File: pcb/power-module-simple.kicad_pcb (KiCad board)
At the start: 4 copper layers, 55 x 55 mm, 43 parts, among them J1 USB_C_PowerOnly_6P, J2 Power, U1 AZ1084-3.3, U2 LM66200DRLR

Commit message: Attribute updates; generated production files
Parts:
- R3, R4: footprint Resistor_SMD:R_0805_2012Metric -> Resistor_SMD:R_0603_1608Metric
- moved FID1 47.0 mm to (54.0, 156.0)

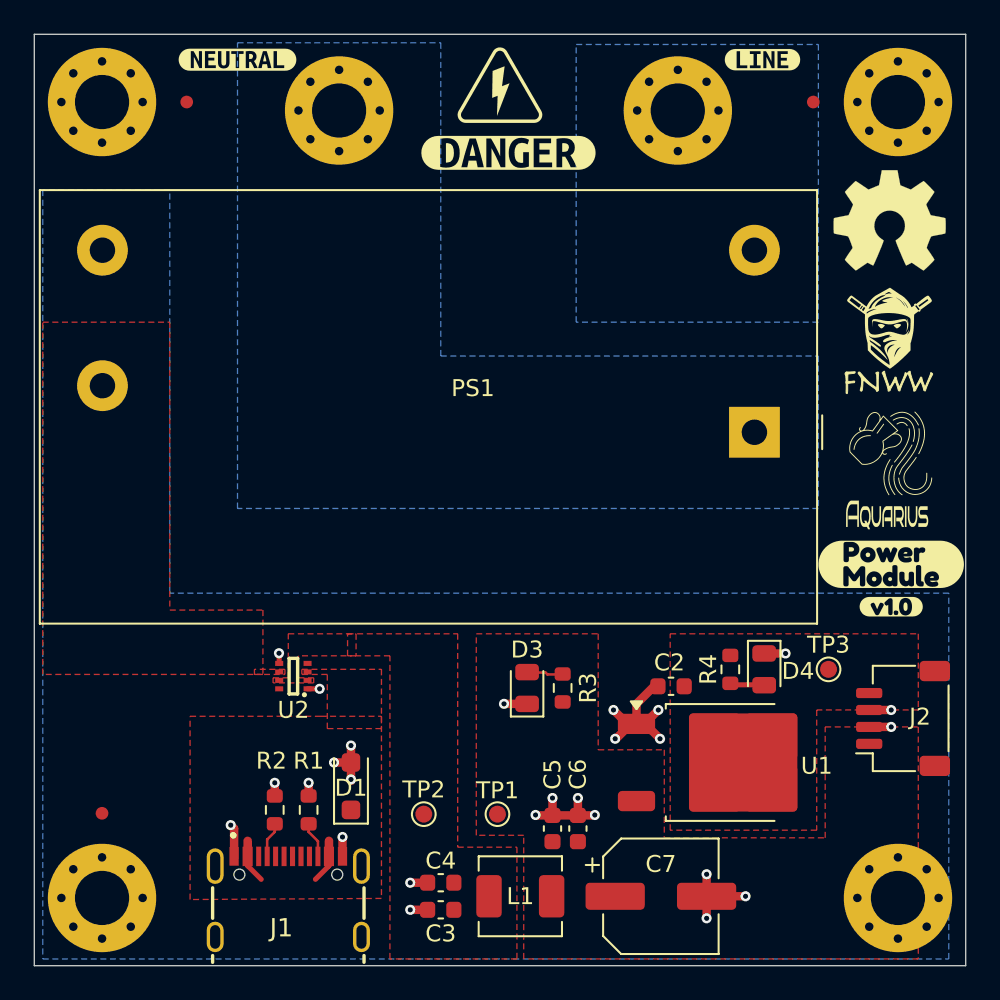
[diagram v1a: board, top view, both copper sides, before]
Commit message: Updated silkscreen and LED size
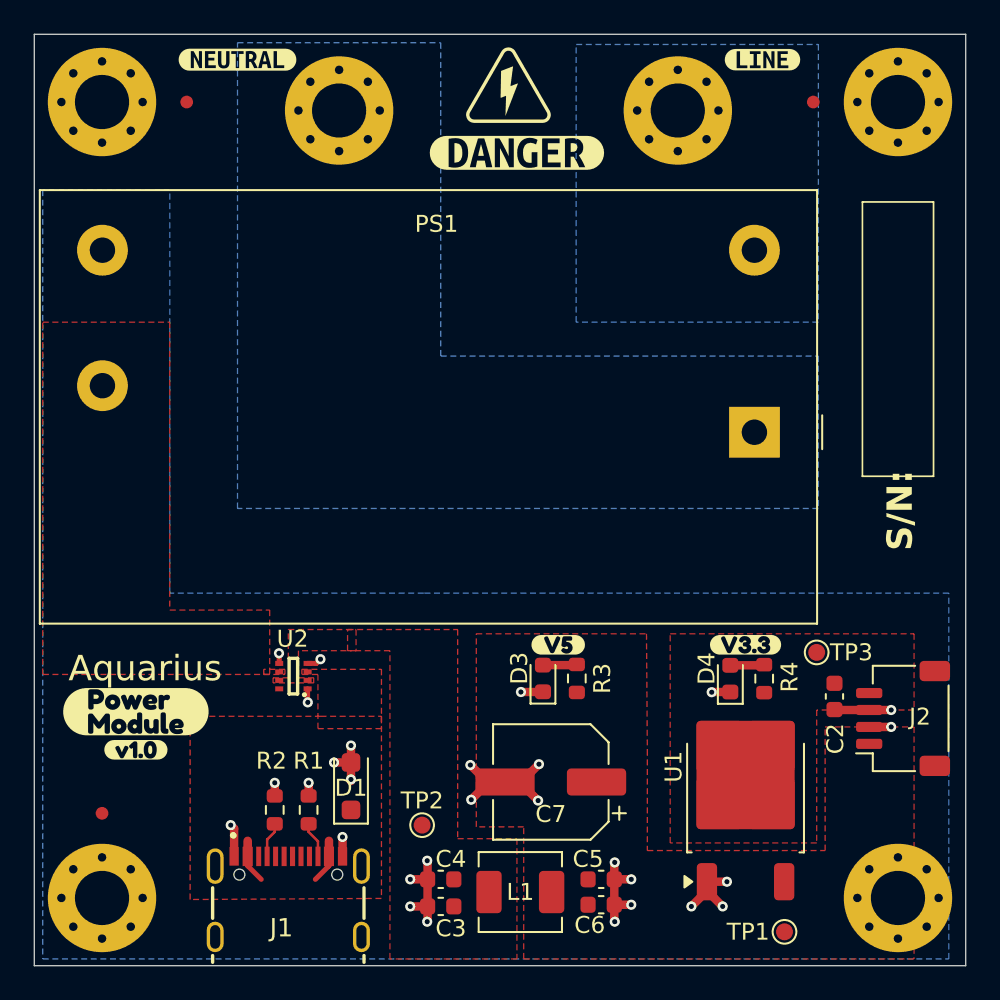
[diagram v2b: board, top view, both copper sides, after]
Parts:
- removed LOGO4: ~, CRGM Logos:FNWW Name 2mmx5mm
- removed LOGO5: ~, CRGM Logos:Aquarius Name 2mmx5mm
- added S2: ~, CRGM Symbols:HIGH-VOLTAGE-5MM, F.Cu at (78.0, 113.0)
- added kibuzzard-67F86A71: G***, kibuzzard-67F86A71, F.Cu at (92.0, 146.1)
- added kibuzzard-67F86A7A: G***, kibuzzard-67F86A7A, F.Cu at (80.9, 146.1)
- added kibuzzard-67F873C9: G***, kibuzzard-67F873C9, B.Cu at (77.5, 142.2)
- added kibuzzard-67F873E4: G***, kibuzzard-67F873E4, B.Cu at (77.5, 146.2)
- D3, D4: footprint LED_SMD:LED_0805_2012Metric -> LED_SMD:LED_0603_1608Metric
- LOGO1: value Logo_Open_Hardware_Small -> ~; footprint Symbol:OSHW-Symbol_6.7x6mm_SilkScreen -> CRGM Logos:FNWW Face 10mm; moved to B.Cu
- LOGO2: value ~ -> Logo_Open_Hardware_Small; footprint CRGM Logos:Aquarius Logo 5mm -> Symbol:OSHW-Logo_5.7x6mm_SilkScreen; moved to B.Cu
- LOGO3: footprint CRGM Logos:FNWW Face 5mm -> CRGM Logos:Aquarius Logo 10mm; moved to B.Cu
- S1: moved to B.Cu
- moved kibuzzard-67E32962 45.4 mm to (56.0, 150.0)
- moved kibuzzard-67E31E9F 45.4 mm to (56.0, 152.2)
- moved LOGO3 28.4 mm to (73.0, 136.9), turned to 180 degrees
- moved LOGO1 23.1 mm to (83.3, 136.5), turned to 180 degrees
- moved TP1 18.3 mm to (94.3, 163.0)
- moved C2 9.67 mm to (97.2, 149.1), turned to -90 degrees
- moved C7 9.37 mm to (80.5, 154.2), turned to 180 degrees
- moved LOGO2 8.09 mm to (94.6, 143.0), turned to 180 degrees
- moved C6 4.71 mm to (83.5, 161.4), turned to 0 degrees
- moved C5 4.16 mm to (83.5, 159.9), turned to 0 degrees
- moved kibuzzard-67E1D06C 2.96 mm to (78.5, 117.0), turned to 180 degrees
- moved U1 2.44 mm to (92.0, 155.0), turned to 90 degrees
- moved D4 2.07 mm to (91.1, 148.1), turned to 90 degrees
- moved R4 2.07 mm to (93.1, 148.1), turned to 90 degrees
- moved TP3 1.22 mm to (96.2, 146.5)
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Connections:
- U2 pad 4: unconnected-(U2-~{ON}-Pad4) -> GND
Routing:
- net GND: track 36.4 -> 43.1 mm, vias 26 -> 29
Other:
- board text added: "Aquarius"
- board text added: "FNWW"
- board text added: "S/N:"

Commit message: Changed switching mechanism; updated power delivery for v3.3
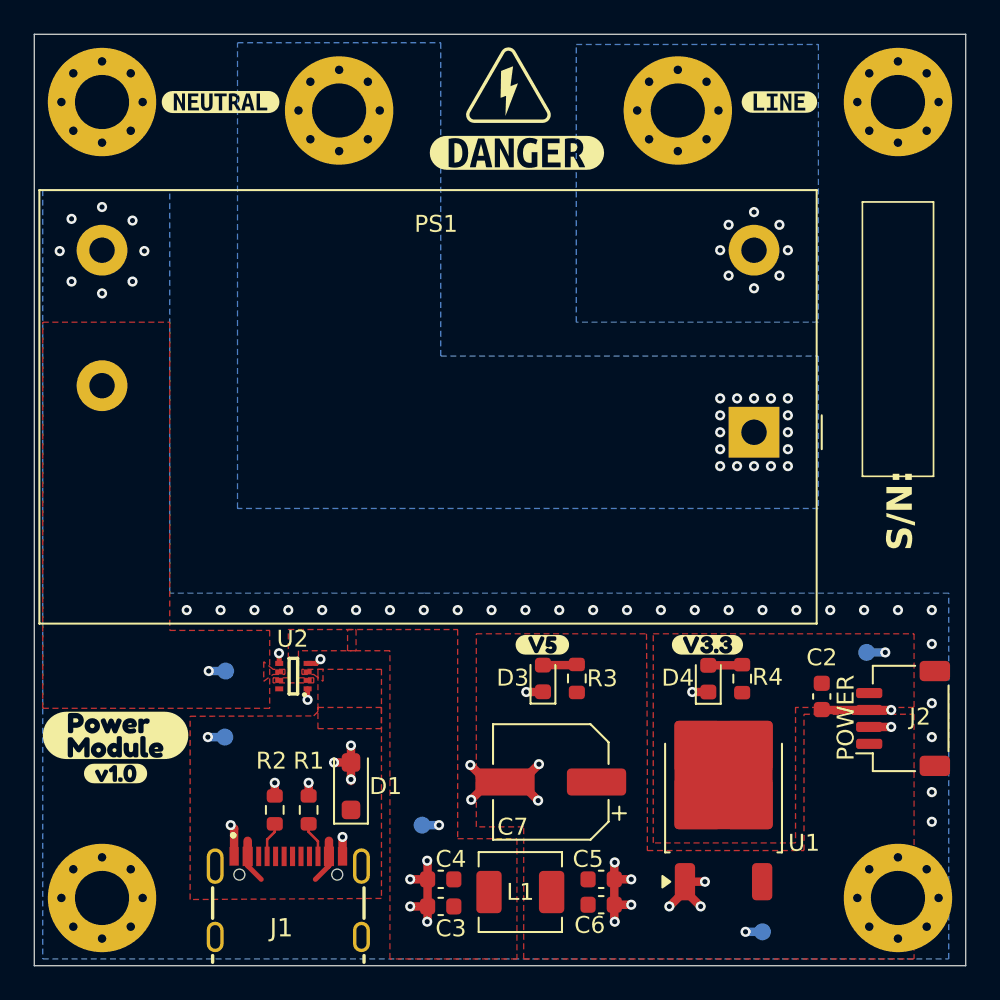
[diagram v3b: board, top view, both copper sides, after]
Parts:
- removed FID1, FID2, FID3: Fiducial, Fiducial:Fiducial_0.75mm_Mask1.5mm
- removed kibuzzard-67F465BD: G***, kibuzzard-67F465BD
- added TP4: LINE_5V, TestPoint:TestPoint_Pad_D1.0mm, B.Cu at (61.3, 147.6)
- added TP5: USB_5V, TestPoint:TestPoint_Pad_D1.0mm, B.Cu at (61.2, 151.5)
- added kibuzzard-68084394: G***, kibuzzard-68084394, F.Cu at (61.0, 114.0)
- added kibuzzard-6810421E: G***, kibuzzard-6810421E, B.Cu at (61.3, 146.1)
- added kibuzzard-6810424A: G***, kibuzzard-6810424A, B.Cu at (72.8, 155.1)
- added kibuzzard-68104254: G***, kibuzzard-68104254, B.Cu at (61.3, 149.9)
- added kibuzzard-6810427B: G***, kibuzzard-6810427B, B.Cu at (99.1, 148.1)
- added kibuzzard-68104292: G***, kibuzzard-68104292, B.Cu at (92.9, 161.3)
- TP1, TP3: moved to B.Cu
- TP2: value V5_RAW -> RAW_5V; moved to B.Cu
- moved LOGO2 34.7 mm to (60.0, 140.8)
- moved TP3 2.95 mm to (99.2, 146.5), turned to 180 degrees
- moved kibuzzard-67F465A8 2.69 mm to (94.0, 114.0)
- moved LOGO1 2.25 mm to (83.3, 134.2)
- moved LOGO3 2.25 mm to (73.0, 134.7)
- moved kibuzzard-67F86A71 2.25 mm to (89.8, 146.1)
- moved kibuzzard-67F873C9 2.25 mm to (77.5, 140.0)
- moved kibuzzard-67F873E4 2.25 mm to (77.5, 144.0)
- moved kibuzzard-67E31E9F 1.84 mm to (54.8, 153.7)
- moved kibuzzard-67E32962 1.84 mm to (54.8, 151.4)
- moved D4 1.30 mm to (89.8, 148.1)
- moved R4 1.30 mm to (91.8, 148.1)
- moved TP1 1.30 mm to (93.0, 163.0), turned to 180 degrees
- moved U1 1.30 mm to (90.7, 155.0)
- moved kibuzzard-67F86A7A 0.94 mm to (80.0, 146.1)
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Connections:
- net 5V_RAW renamed RAW_5V
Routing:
- net +3.3V: track 0.02 -> 1.10 mm, vias 0 -> 1
- net USB_5V: track 5.34 -> 6.34 mm, vias 0 -> 1
- net RAW_5V: track 0.00 -> 1.00 mm, vias 0 -> 1
- net LINE_5V: track 0.00 -> 1.00 mm, vias 0 -> 1
- net +5V: track 0.00 -> 1.00 mm, vias 0 -> 1
- net GND: track 43.1 -> 43.2 mm, vias 29 -> 65
- net /AC_N: vias 0 -> 16
- net /AC_L: vias 0 -> 8
- added copper zone on In2.Cu, net /AC_L
- added copper zone on In2.Cu, net /AC_N
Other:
- board text added: "POWER"

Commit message: Fixed AZ1084 footprint
Fixed USB-C Connector / symbol mismatch
Moved parts around
Moved USB-C connector from overhanging.
Generated ibom.
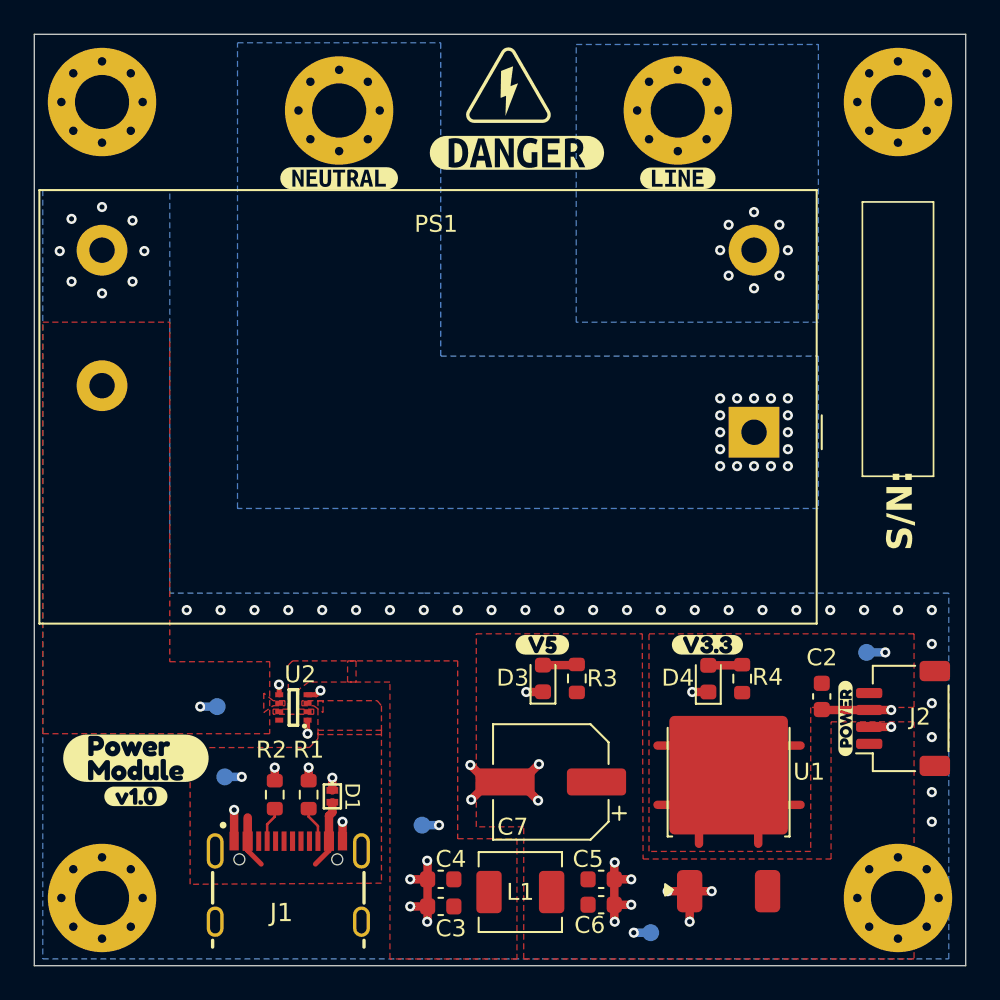
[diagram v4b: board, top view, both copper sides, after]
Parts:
- added kibuzzard-681BE833: G***, kibuzzard-681BE833, F.Cu at (97.9, 150.4)
- D1: value SMF6V5A -> PESD5V5C1BL; footprint Diode_SMD:D_SOD-123F -> CRGM Passive:DFN1006-2
- U1: footprint Package_TO_SOT_SMD:TO-252-2 -> CRGM Power:TO-252-2
- moved kibuzzard-68084394 8.32 mm to (68.0, 118.5)
- moved kibuzzard-67F465A8 7.50 mm to (88.0, 118.5)
- moved LOGO2 7.32 mm to (61.0, 133.5)
- moved TP1 6.60 mm to (86.4, 163.1)
- moved kibuzzard-68104254 2.41 mm to (60.8, 152.2)
- moved TP5 2.35 mm to (61.2, 153.8)
- moved kibuzzard-67F873E4 2.25 mm to (77.5, 146.2)
- moved TP4 2.16 mm to (60.8, 149.7)
- moved kibuzzard-6810421E 1.97 mm to (60.8, 148.0)
- moved U2 1.85 mm to (65.3, 149.8)
- moved kibuzzard-67E31E9F 1.81 mm to (56.0, 155.0)
- moved kibuzzard-67E32962 1.81 mm to (56.0, 152.8)
- moved kibuzzard-67F873C9 1.75 mm to (77.5, 141.8)
- moved U1 1.29 mm to (91.0, 153.8)
- moved D1 1.25 mm to (67.6, 155.0), turned to -90 degrees
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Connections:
- D1 pad 1: USB_5V -> GND
- D1 pad 2: GND -> USB_5V
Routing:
- net +3.3V: track 1.10 -> 15.6 mm
- net GND: track 43.2 -> 40.5 mm, vias 65 -> 63
- net USB_5V: track 6.34 -> 8.28 mm
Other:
- board text removed: "POWER"
